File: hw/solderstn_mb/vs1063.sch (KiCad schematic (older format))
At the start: 49 parts, among them U1901 TLV1117LV18DCY, U1902 TS5A3159A, U1903 VS1063a, U1904 TS5A3159A, Y1901 12.288M

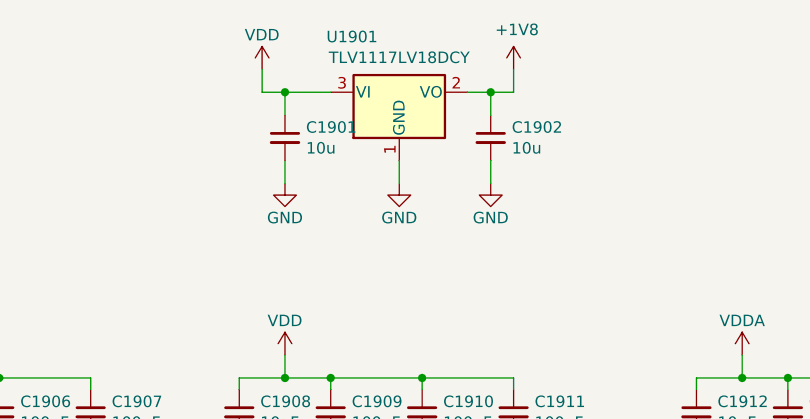
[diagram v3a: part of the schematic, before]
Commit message: MainBoard: change fp for all 3225 oscillators to normal (was -Handsoldering)
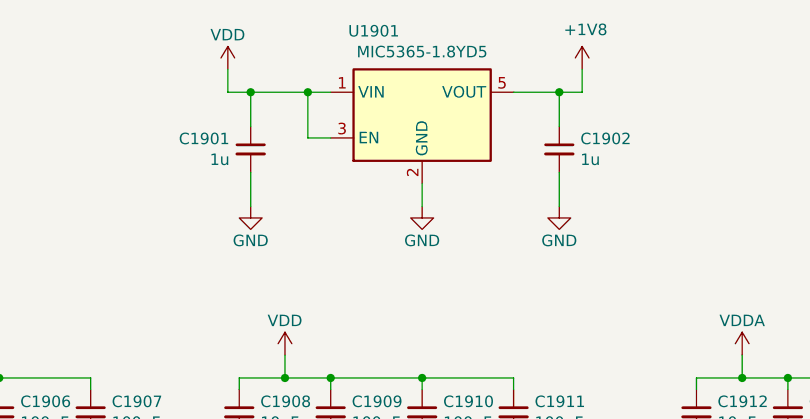
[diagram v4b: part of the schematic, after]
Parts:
- removed U1901: TLV1117LV18DCY, Package_TO_SOT_SMD:SOT-223-3_TabPin2, symbol customlib_mj:TLV1117LV30DCY
- added U1901: MIC5365-1.8YD5, Package_TO_SOT_SMD:SOT-23-5, symbol customlib_mj:MIC5365-1.8YD5
- C1901, C1902: value 10u -> 1u
- Y1901: footprint Crystal:Crystal_SMD_SeikoEpson_TSX3225-4Pin_3.2x2.5mm_HandSoldering -> Crystal:Crystal_SMD_SeikoEpson_TSX3225-4Pin_3.2x2.5mm
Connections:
- net +1V8: now also U1901.5 (VOUT)
- net AGND: now also U1901.2 (GND)
- net IOVDD: now also U1901.1 (VIN), U1901.3 (EN)
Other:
- moved on the sheet: C1901, C1902
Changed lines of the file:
@@
 F 0 "Y1901" V 1304 4903 50  0000 L CNN
 F 1 "12.288M" V 1395 4903 50  0000 L CNN
-F 2 "Crystal:Crystal_SMD_SeikoEpson_TSX3225-4Pin_3.2x2.5mm_HandSoldering" H 1350 4800 50  0001 C CNN
+F 2 "Crystal:Crystal_SMD_SeikoEpson_TSX3225-4Pin_3.2x2.5mm" H 1350 4800 50  0001 C CNN
 F 3 "https://www.mouser.se/datasheet/2/122/ecx-32-1100709.pdf" H 1350 4800 50  0001 C CNN
 	1    1350 4800
@@
 	4800 4000 5600 4000
 $Comp
-L customlib_mj:TLV1117LV30DCY U?
-U 1 1 5FC8C0CC
-P 4150 1250
-AR Path="/5F472B62/5FC8C0CC" Ref="U?"  Part="1"
-AR Path="/5FAFD5BA/5FEE4431/5FC8C0CC" Ref="U1901"  Part="1"
-F 0 "U1901" H 3831 1492 50  0000 L CNN
-F 1 "TLV1117LV18DCY" H 4150 1401 50  0000 C CNN
-F 2 "Package_TO_SOT_SMD:SOT-223-3_TabPin2" H 4150 1050 50  0001 C CNN
-F 3 "https://www.ti.com/lit/gpn/tlv1117lv" H 4150 1250 50  0001 C CNN
-	1    4150 1250
-	1    0    0    -1
-$EndComp
-$Comp
 L Device:C_Small C?
 U 1 1 5FC8C0D2
-P 3650 1450
+P 3500 1500
 AR Path="/5F472B62/5FC8C0D2" Ref="C?"  Part="1"
 AR Path="/5FAFD5BA/5FEE4431/5FC8C0D2" Ref="C1901"  Part="1"
-F 0 "C1901" H 3742 1496 50  0000 L CNN
-F 1 "10u" H 3742 1405 50  0000 L CNN
-F 2 "Capacitor_SMD:C_0603_1608Metric" H 3650 1450 50  0001 C CNN
-F 3 "~" H 3650 1450 50  0001 C CNN
-	1    3650 1450
-	1    0    0    -1
+F 0 "C1901" H 3592 1546 50  0000 L CNN
+F 1 "1u" H 3592 1455 50  0000 L CNN
+F 2 "Capacitor_SMD:C_0603_1608Metric" H 3500 1500 50  0001 C CNN
+F 3 "~" H 3500 1500 50  0001 C CNN
+	1    3500 1500
+	-1   0    0    -1
 $EndComp
 $Comp
 L Device:C_Small C?
 U 1 1 5FC8C0D8
-P 4550 1450
+P 4850 1500
 AR Path="/5F472B62/5FC8C0D8" Ref="C?"  Part="1"
 AR Path="/5FAFD5BA/5FEE4431/5FC8C0D8" Ref="C1902"  Part="1"
-F 0 "C1902" H 4642 1496 50  0000 L CNN
-F 1 "10u" H 4642 1405 50  0000 L CNN
-F 2 "Capacitor_SMD:C_0603_1608Metric" H 4550 1450 50  0001 C CNN
-F 3 "~" H 4550 1450 50  0001 C CNN
-	1    4550 1450
+F 0 "C1902" H 4942 1546 50  0000 L CNN
+F 1 "1u" H 4942 1455 50  0000 L CNN
+F 2 "Capacitor_SMD:C_0603_1608Metric" H 4850 1500 50  0001 C CNN
+F 3 "~" H 4850 1500 50  0001 C CNN
+	1    4850 1500
 	1    0    0    -1
 $EndComp
@@
 L power:GND #PWR?
 U 1 1 5FC8C0DE
-P 3650 1650
+P 3500 1750
 AR Path="/5F472B62/5FC8C0DE" Ref="#PWR?"  Part="1"
 AR Path="/5FAFD5BA/5FEE4431/5FC8C0DE" Ref="#PWR01903"  Part="1"
-F 0 "#PWR01903" H 3650 1400 50  0001 C CNN
-F 1 "GND" H 3650 1500 50  0000 C CNN
-F 2 "" H 3650 1650 50  0001 C CNN
-F 3 "" H 3650 1650 50  0001 C CNN
-	1    3650 1650
+F 0 "#PWR01903" H 3500 1500 50  0001 C CNN
+F 1 "GND" H 3500 1600 50  0000 C CNN
+F 2 "" H 3500 1750 50  0001 C CNN
+F 3 "" H 3500 1750 50  0001 C CNN
+	1    3500 1750
 	1    0    0    -1
 $EndComp
@@
 L power:GND #PWR?
 U 1 1 5FC8C0E4
-P 4150 1650
+P 4250 1750
 AR Path="/5F472B62/5FC8C0E4" Ref="#PWR?"  Part="1"
 AR Path="/5FAFD5BA/5FEE4431/5FC8C0E4" Ref="#PWR01904"  Part="1"
-F 0 "#PWR01904" H 4150 1400 50  0001 C CNN
-F 1 "GND" H 4150 1500 50  0000 C CNN
-F 2 "" H 4150 1650 50  0001 C CNN
-F 3 "" H 4150 1650 50  0001 C CNN
-	1    4150 1650
+F 0 "#PWR01904" H 4250 1500 50  0001 C CNN
+F 1 "GND" H 4250 1600 50  0000 C CNN
+F 2 "" H 4250 1750 50  0001 C CNN
+F 3 "" H 4250 1750 50  0001 C CNN
+	1    4250 1750
 	1    0    0    -1
 $EndComp
@@
 L power:GND #PWR?
 U 1 1 5FC8C0EA
-P 4550 1650
+P 4850 1750
 AR Path="/5F472B62/5FC8C0EA" Ref="#PWR?"  Part="1"
 AR Path="/5FAFD5BA/5FEE4431/5FC8C0EA" Ref="#PWR01905"  Part="1"
-F 0 "#PWR01905" H 4550 1400 50  0001 C CNN
-F 1 "GND" H 4550 1500 50  0000 C CNN
-F 2 "" H 4550 1650 50  0001 C CNN
-F 3 "" H 4550 1650 50  0001 C CNN
-	1    4550 1650
-	1    0    0    -1
-$EndComp
-Wire Wire Line
-	3550 1150 3550 1250
-Wire Wire Line
-	3550 1250 3650 1250
-Wire Wire Line
-	3650 1250 3650 1350
-Connection ~ 3650 1250
-Wire Wire Line
-	3650 1250 3850 1250
-Wire Wire Line
-	3650 1550 3650 1650
-Wire Wire Line
-	4150 1550 4150 1650
-Wire Wire Line
-	4450 1250 4550 1250
-Wire Wire Line
-	4650 1250 4650 1150
-Wire Wire Line
-	4550 1250 4550 1350
-Connection ~ 4550 1250
-Wire Wire Line
-	4550 1250 4650 1250
-Wire Wire Line
-	4550 1550 4550 1650
+F 0 "#PWR01905" H 4850 1500 50  0001 C CNN
+F 1 "GND" H 4850 1600 50  0000 C CNN
+F 2 "" H 4850 1750 50  0001 C CNN
+F 3 "" H 4850 1750 50  0001 C CNN
+	1    4850 1750
+	1    0    0    -1
+$EndComp
+Wire Wire Line
+	3400 1150 3400 1250
+Wire Wire Line
+	3400 1250 3500 1250
+Wire Wire Line
+	3500 1250 3500 1400
+Connection ~ 3500 1250
+Wire Wire Line
+	3500 1250 3750 1250
+Wire Wire Line
+	3500 1600 3500 1750
+Wire Wire Line
+	4250 1650 4250 1750
+Wire Wire Line
+	4650 1250 4850 1250
+Wire Wire Line
+	4950 1250 4950 1150
+Wire Wire Line
+	4850 1250 4850 1400
+Connection ~ 4850 1250
+Wire Wire Line
+	4850 1250 4950 1250
+Wire Wire Line
+	4850 1600 4850 1750
 $Comp
 L power:+1V8 #PWR01902
 U 1 1 5FCB4EA0
-P 4650 1150
-F 0 "#PWR01902" H 4650 1000 50  0001 C CNN
-F 1 "+1V8" H 4665 1323 50  0000 C CNN
-F 2 "" H 4650 1150 50  0001 C CNN
-F 3 "" H 4650 1150 50  0001 C CNN
-	1    4650 1150
+P 4950 1150
+F 0 "#PWR01902" H 4950 1000 50  0001 C CNN
+F 1 "+1V8" H 4965 1323 50  0000 C CNN
+F 2 "" H 4950 1150 50  0001 C CNN
+F 3 "" H 4950 1150 50  0001 C CNN
+	1    4950 1150
 	1    0    0    -1
 $EndComp
@@
 L power:VDD #PWR01901
 U 1 1 5FCB5487
-P 3550 1150
-F 0 "#PWR01901" H 3550 1000 50  0001 C CNN
-F 1 "VDD" H 3550 1300 50  0000 C CNN
-F 2 "" H 3550 1150 50  0001 C CNN
-F 3 "" H 3550 1150 50  0001 C CNN
-	1    3550 1150
+P 3400 1150
+F 0 "#PWR01901" H 3400 1000 50  0001 C CNN
+F 1 "VDD" H 3400 1300 50  0000 C CNN
+F 2 "" H 3400 1150 50  0001 C CNN
+F 3 "" H 3400 1150 50  0001 C CNN
+	1    3400 1150
 	1    0    0    -1
 $EndComp
@@
 Wire Wire Line
 	1300 4100 1750 4100
+$Comp
+L customlib_mj:MIC5365-1.8YD5 U1901
+U 1 1 5FBEF354
+P 4250 1350
+F 0 "U1901" H 3926 1717 50  0000 L CNN
+F 1 "MIC5365-1.8YD5" H 4250 1626 50  0000 C CNN
+F 2 "Package_TO_SOT_SMD:SOT-23-5" H 4250 1700 50  0001 C CNN
+F 3 "http://ww1.microchip.com/downloads/en/DeviceDoc/mic5365.pdf" H 4000 1600 50  0001 C CNN
+	1    4250 1350
+	1    0    0    -1
+$EndComp
+Wire Wire Line
+	3850 1450 3750 1450
+Wire Wire Line
+	3750 1450 3750 1250
+Connection ~ 3750 1250
+Wire Wire Line
+	3750 1250 3850 1250
 $EndSCHEMATC

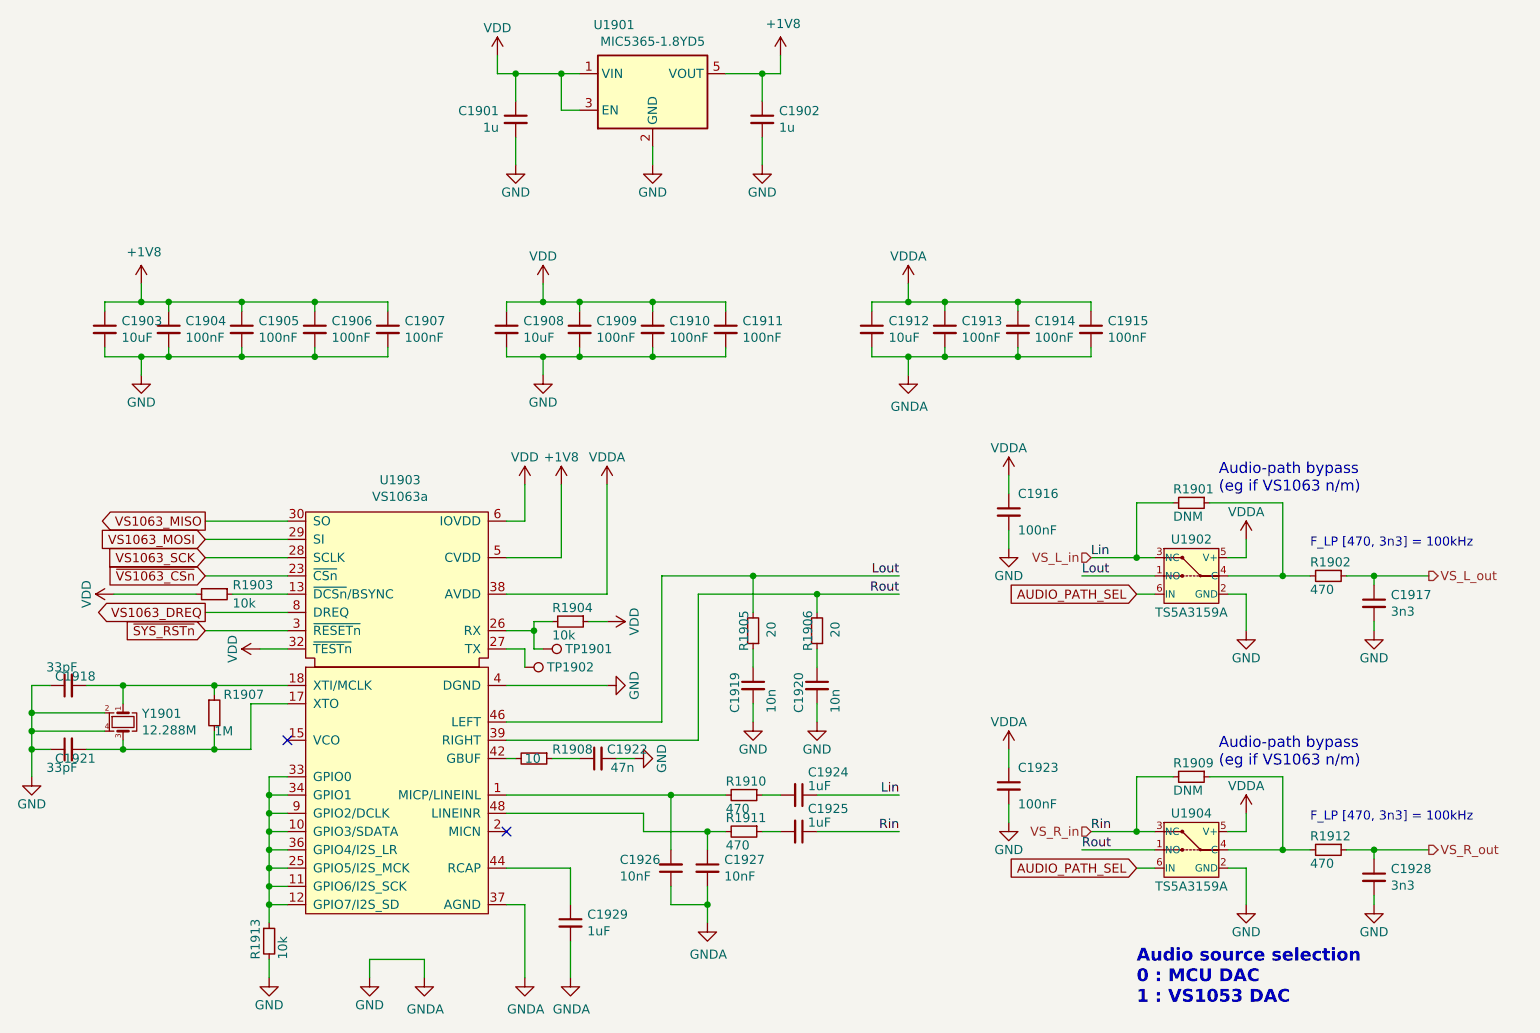
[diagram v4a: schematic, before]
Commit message: Some placement (audio, RTC)
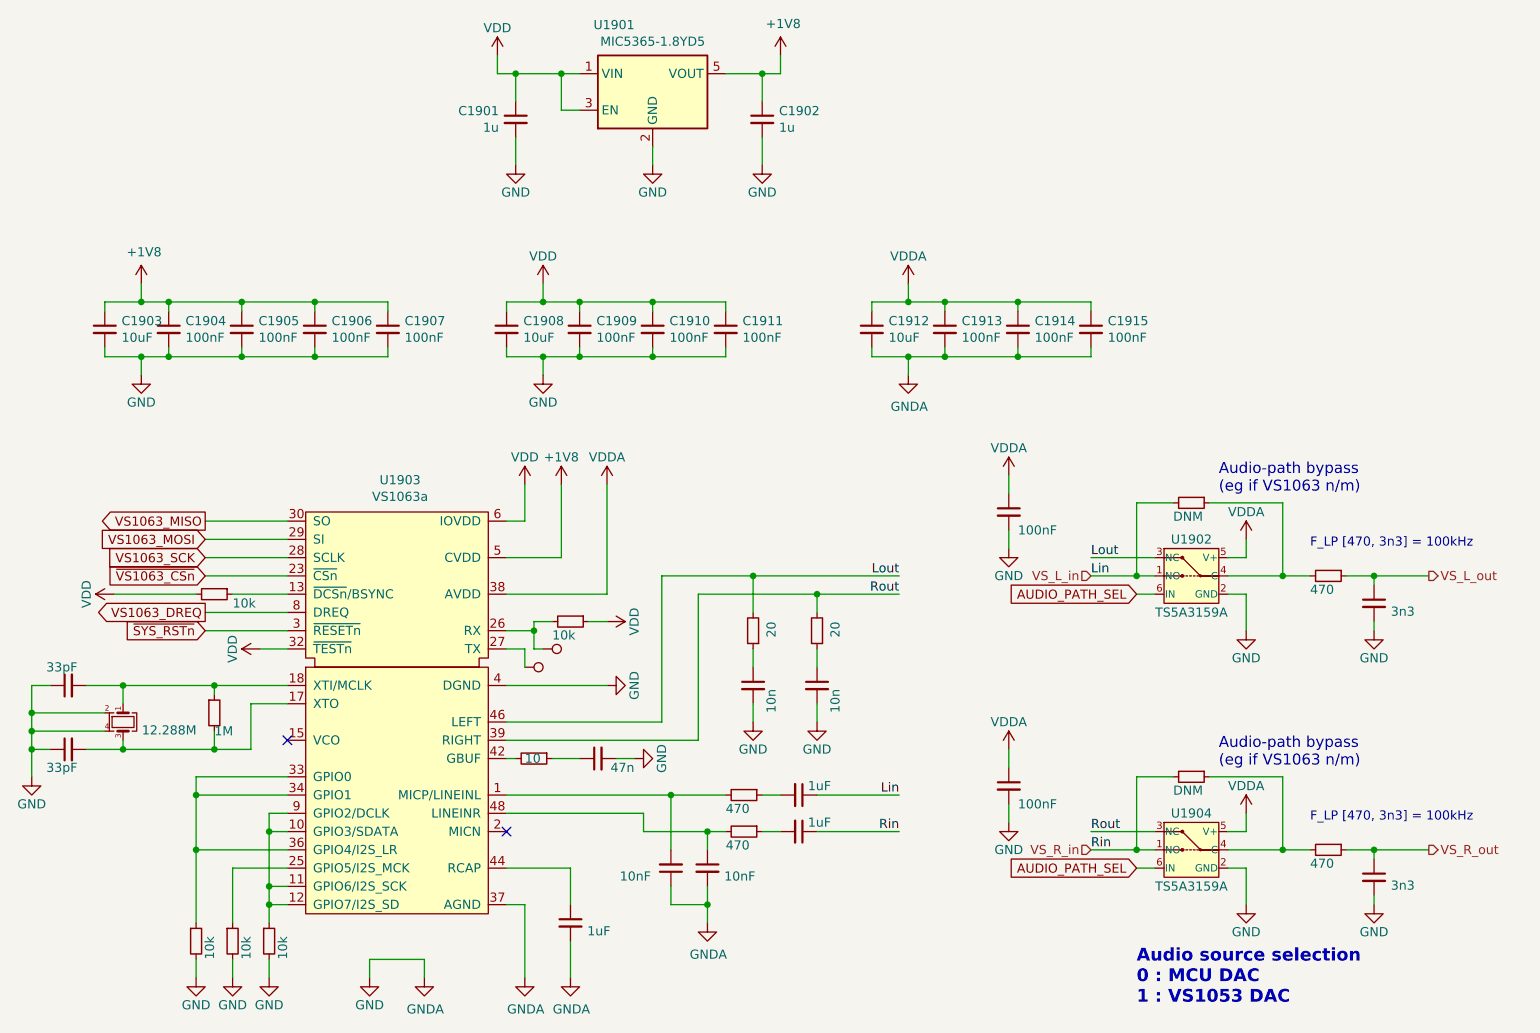
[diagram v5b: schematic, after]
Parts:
- added R1914, R1915: 10k, Resistor_SMD:R_0402_1005Metric, symbol customlib_mj:R_Small
- C1924, C1925: footprint Capacitor_SMD:C_0603_1608Metric -> Capacitor_SMD:C_0402_1005Metric
- R1901, R1909: footprint Resistor_SMD:R_0603_1608Metric -> Resistor_SMD:R_0402_1005Metric
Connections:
- net AGND: now also R1914.2, R1915.2
- net Lout: now also U1902.3 (NC); no longer U1902.1 (NO)
- net Rout: now also U1904.3 (NC); no longer U1904.1 (NO)
- net VS_L_in: now also U1902.1 (NO); no longer U1902.3 (NC)
- net VS_R_in: now also U1904.1 (NO); no longer U1904.3 (NC)
- net at R1913.1, U1903.10 (GPIO3/SDATA), U1903.11 (GPIO6/I2S_SCK)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: no longer U1903.25 (GPIO5/I2S_MCK), U1903.33 (GPIO0), U1903.34 (GPIO1), U1903.36 (GPIO4/I2S_LR)
- new net: R1915.1, U1903.25 (GPIO5/I2S_MCK)
- new net: R1914.1, U1903.33 (GPIO0), U1903.34 (GPIO1), U1903.36 (GPIO4/I2S_LR)

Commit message: MB: major update of footprints, LCSC part numbers and Basic/Extended library indicator, for _most_ of the BoM. (Also removed JP1101/JP1102, bypass jmprs)
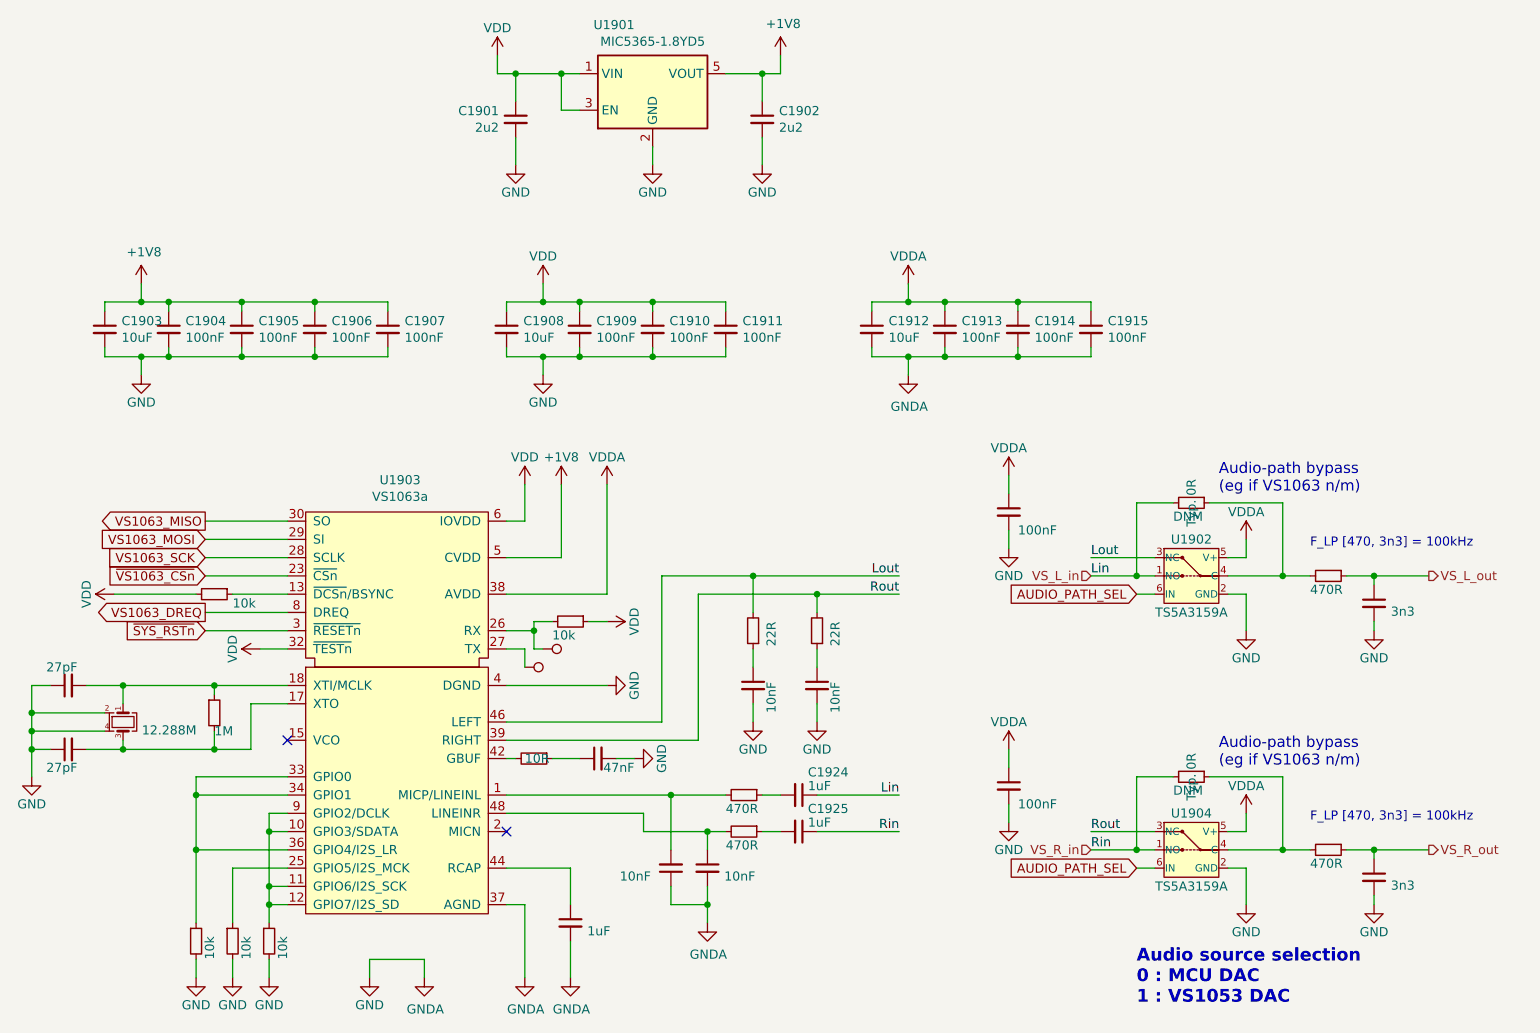
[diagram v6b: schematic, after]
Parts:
- C1901, C1902: value 1u -> 2u2; JLC_part (none) -> Basic; LCSC (none) -> C23630
- C1903, C1908, C1912: footprint Capacitor_SMD:C_0603_1608Metric -> Capacitor_SMD:C_0402_1005Metric; JLC_part (none) -> Basic; LCSC (none) -> C15525
- C1904, C1905, C1906, C1907, C1909, C1910, C1911, C1913, C1914, C1915, C1916, C1923: JLC_part (none) -> Basic; LCSC (none) -> C1525
- C1917, C1928: JLC_part (none) -> Basic; LCSC (none) -> C26404
- C1918, C1921: value 33pF -> 27pF; JLC_part (none) -> Basic; LCSC (none) -> C1557
- C1919, C1920: value 10n -> 10nF; JLC_part (none) -> Basic; LCSC (none) -> C15195
- C1922: value 47n -> 47nF; footprint Capacitor_SMD:C_0402_1005Metric -> Capacitor_SMD:C_0603_1608Metric; JLC_part (none) -> Basic; LCSC (none) -> C1622
- C1924, C1925: footprint Capacitor_SMD:C_0402_1005Metric -> Capacitor_SMD:C_1206_3216Metric; JLC_part (none) -> Basic; LCSC (none) -> C1848
- C1926, C1927: JLC_part (none) -> Basic; LCSC (none) -> C15195
- C1929: footprint Capacitor_SMD:C_0603_1608Metric -> Capacitor_SMD:C_0402_1005Metric; JLC_part (none) -> Basic; LCSC (none) -> C52923
- R1902, R1910, R1911, R1912: value 470 -> 470R; JLC_part (none) -> Basic; LCSC (none) -> C25117
- R1903, R1904, R1913, R1914, R1915: JLC_part (none) -> Basic; LCSC (none) -> C25744
- R1905, R1906: value 20 -> 22R; JLC_part (none) -> Basic; LCSC (none) -> C25092
- R1907: JLC_part (none) -> Basic; LCSC (none) -> C26083
- R1908: value 10 -> 10R; JLC_part (none) -> Basic; LCSC (none) -> C25077
- U1902, U1904: JLC_part (none) -> Extended; LCSC (none) -> C128405
- Y1901: JLC_part (none) -> Extended; LCSC (none) -> C70567

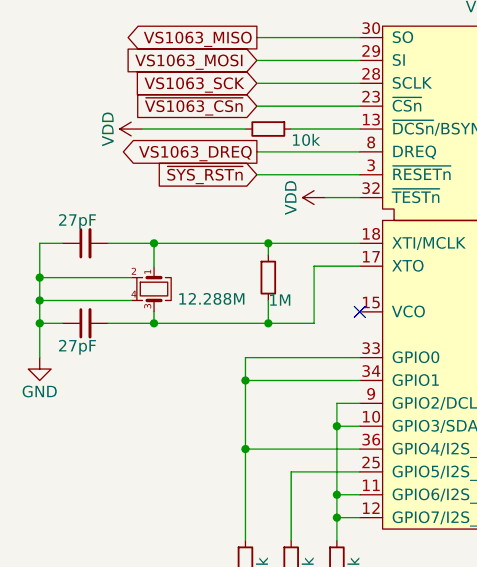
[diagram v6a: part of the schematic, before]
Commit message: MB: update xtal osc load caps from 27pF -> 10pF
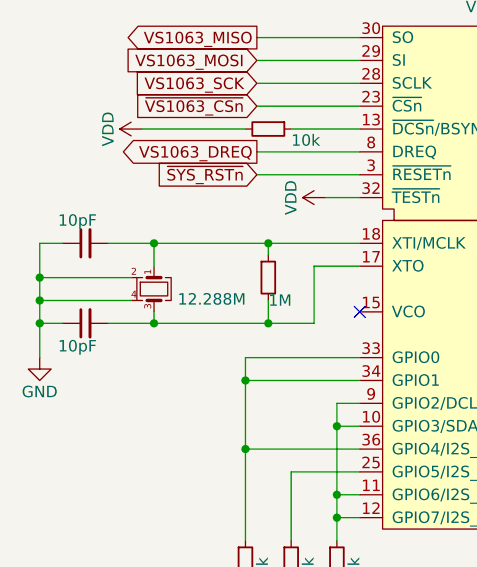
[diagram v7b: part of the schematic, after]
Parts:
- C1918, C1921: value 27pF -> 10pF; LCSC C1557 -> C32949
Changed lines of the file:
@@
 P 1050 4950
 F 0 "C1921" V 1000 4800 50  0001 L CNN
-F 1 "27pF" V 950 4900 50  0000 L CNN
+F 1 "10pF" V 950 4900 50  0000 L CNN
 F 2 "Capacitor_SMD:C_0402_1005Metric" H 1050 4950 50  0001 C CNN
 F 3 "~" H 1050 4950 50  0001 C CNN
 F 4 "Basic" H 1050 4950 50  0001 C CNN "JLC_part"
-F 5 "C1557" H 1050 4950 50  0001 C CNN "LCSC"
+F 5 "C32949" H 1050 4950 50  0001 C CNN "LCSC"
 	1    1050 4950
 	0    -1   -1   0
@@
 P 1050 4600
 F 0 "C1918" V 1100 4450 50  0001 L CNN
-F 1 "27pF" V 1150 4550 50  0000 L CNN
+F 1 "10pF" V 1150 4550 50  0000 L CNN
 F 2 "Capacitor_SMD:C_0402_1005Metric" H 1050 4600 50  0001 C CNN
 F 3 "~" H 1050 4600 50  0001 C CNN
 F 4 "Basic" H 1050 4600 50  0001 C CNN "JLC_part"
-F 5 "C1557" H 1050 4600 50  0001 C CNN "LCSC"
+F 5 "C32949" H 1050 4600 50  0001 C CNN "LCSC"
 	1    1050 4600
 	0    -1   -1   0
